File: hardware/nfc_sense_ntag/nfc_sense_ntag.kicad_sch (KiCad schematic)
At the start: 16 parts, among them U1 TMP117AIDRVR

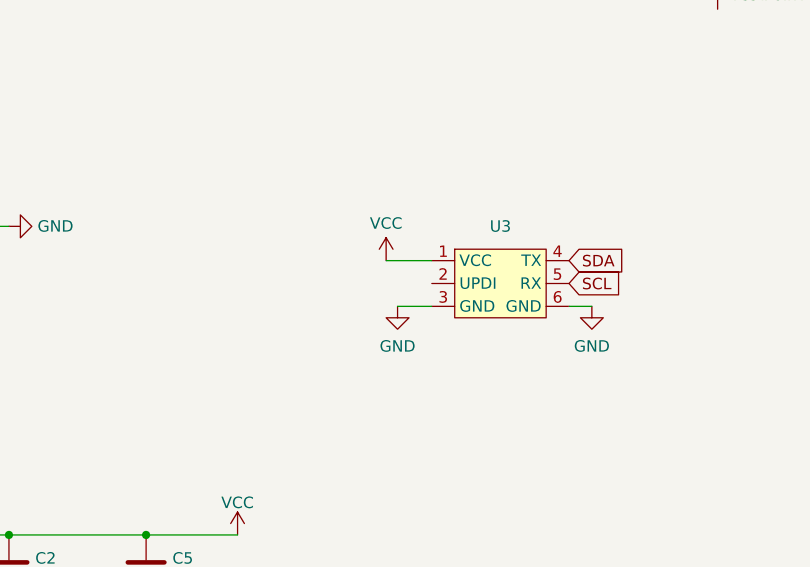
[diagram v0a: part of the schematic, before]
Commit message: update 3D transparency for knife version
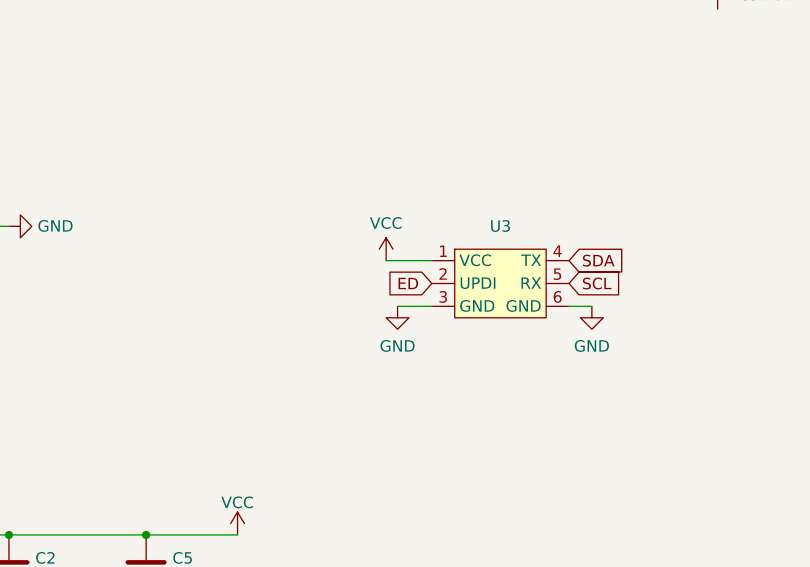
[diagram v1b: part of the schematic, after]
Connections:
- net ED: now also U3.2 (UPDI)
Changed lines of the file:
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@@
+		)
+	)
+	(global_label "ED"
+		(shape input)
+		(at 189.23 120.65 180)
+		(fields_autoplaced yes)
+		(effects
+			(font
+				(size 1.27 1.27)
+			)
+			(justify right)
+		)
+		(property "Intersheetrefs" "${INTERSHEET_REFS}"
+			(at 183.8258 120.65 0)
+			(effects
+				(font
+					(size 1.27 1.27)
+				)
+				(justify right)
+				(hide yes)
+			)
 		)
 	)
